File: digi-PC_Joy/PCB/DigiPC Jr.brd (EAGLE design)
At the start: 42.7 x 24.8 mm, 7 parts

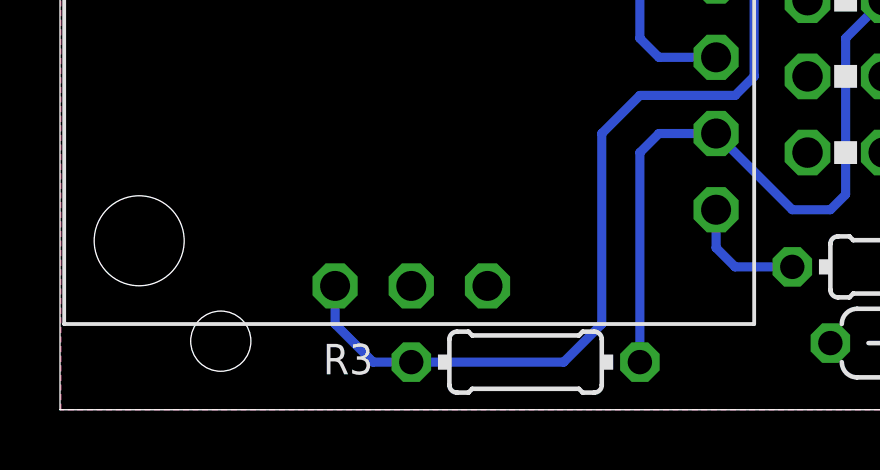
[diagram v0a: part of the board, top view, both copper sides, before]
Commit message: Updadet footprint of digispark board with USB connector
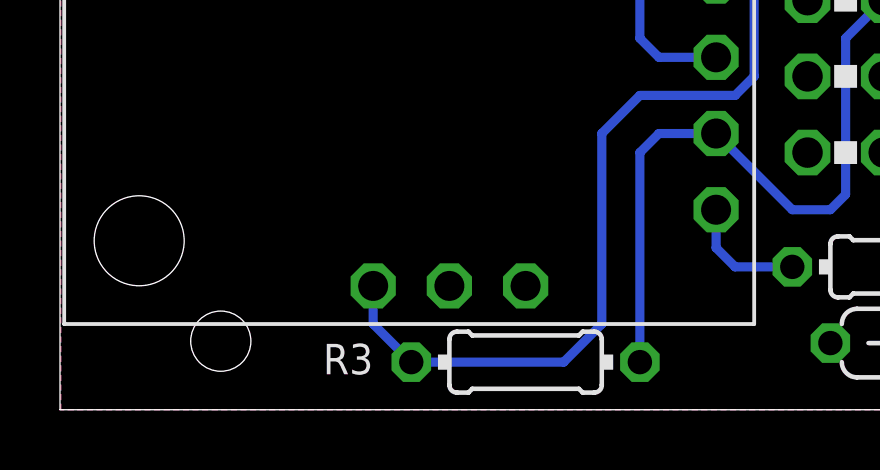
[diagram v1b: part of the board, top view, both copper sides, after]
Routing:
- net VCC: track 29.2 -> 28.0 mm
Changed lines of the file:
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@@
 <contactref element="R3" pad="2"/>
 <contactref element="B1" pad="5V"/>
-<wire x1="16.51" y1="12.065" x2="16.51" y2="10.795" width="0.3048" layer="16"/>
-<wire x1="16.51" y1="10.795" x2="17.78" y2="9.525" width="0.3048" layer="16"/>
-<wire x1="17.78" y1="9.525" x2="19.05" y2="9.525" width="0.3048" layer="16"/>
+<wire x1="17.78" y1="12.065" x2="17.78" y2="10.795" width="0.3048" layer="16"/>
+<wire x1="17.78" y1="10.795" x2="19.05" y2="9.525" width="0.3048" layer="16"/>
 <wire x1="32.258" y1="24.13" x2="30.48" y2="22.352" width="0.3048" layer="16"/>
 <wire x1="30.48" y1="22.352" x2="30.48" y2="19.05" width="0.3048" layer="16"/>

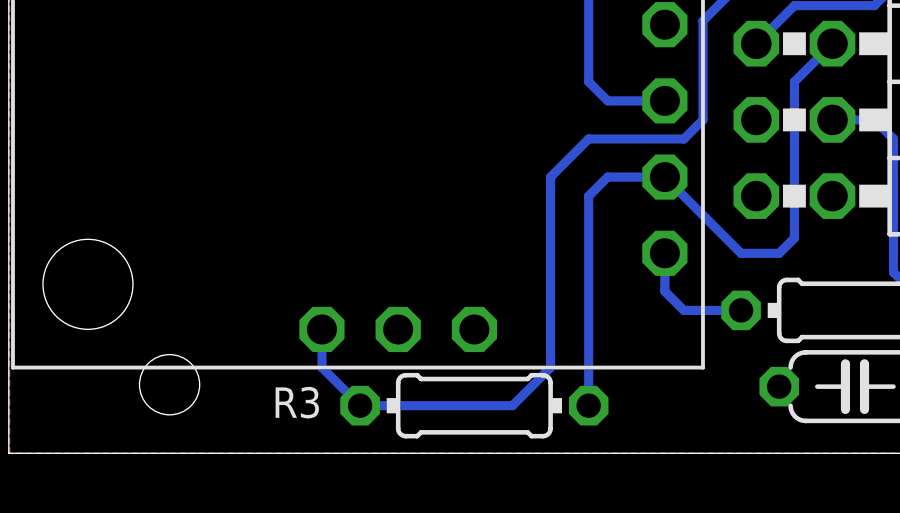
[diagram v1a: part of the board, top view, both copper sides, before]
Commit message: updated digispark footprint
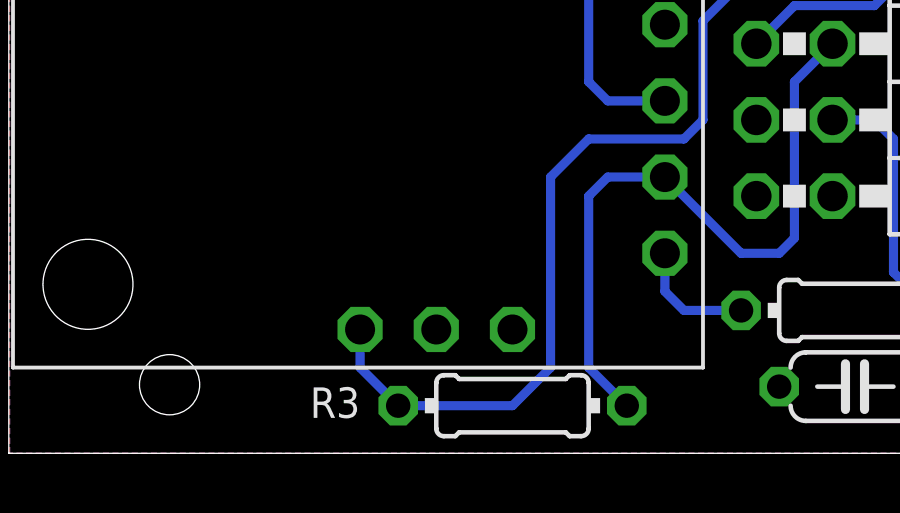
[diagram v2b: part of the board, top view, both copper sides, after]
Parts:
- moved R3 1.27 mm to (24.1, 9.53)
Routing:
- net VCC: track 28.0 -> 26.7 mm
- net S2: track 22.4 -> 22.9 mm
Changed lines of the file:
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@@
 <attribute name="VALUE" x="34.5694" y="27.4574" size="1.016" layer="27" ratio="10"/>
 </element>
-<element name="R3" library="rcl" package="0204/7" value="560" x="22.86" y="9.525" smashed="yes" rot="R180">
-<attribute name="NAME" x="17.78" y="10.1346" size="1.016" layer="25" ratio="10" rot="R180"/>
-<attribute name="VALUE" x="21.8694" y="9.0424" size="1.016" layer="27" ratio="10"/>
+<element name="R3" library="rcl" package="0204/7" value="560" x="24.13" y="9.525" smashed="yes" rot="R180">
+<attribute name="NAME" x="19.05" y="10.1346" size="1.016" layer="25" ratio="10" rot="R180"/>
+<attribute name="VALUE" x="23.1394" y="9.0424" size="1.016" layer="27" ratio="10"/>
 </element>
 <element name="B1" library="Digistump" package="DIGISPARK_SOCKET" value="" x="30.48" y="29.845" smashed="yes" rot="R270">
@@
 <contactref element="R3" pad="2"/>
 <contactref element="B1" pad="5V"/>
-<wire x1="17.78" y1="12.065" x2="17.78" y2="10.795" width="0.3048" layer="16"/>
-<wire x1="17.78" y1="10.795" x2="19.05" y2="9.525" width="0.3048" layer="16"/>
+<wire x1="19.05" y1="12.065" x2="19.05" y2="10.795" width="0.3048" layer="16"/>
+<wire x1="19.05" y1="10.795" x2="20.32" y2="9.525" width="0.3048" layer="16"/>
 <wire x1="32.258" y1="24.13" x2="30.48" y2="22.352" width="0.3048" layer="16"/>
 <wire x1="30.48" y1="22.352" x2="30.48" y2="19.05" width="0.3048" layer="16"/>
@@
 <wire x1="25.4" y1="17.145" x2="25.4" y2="10.795" width="0.3048" layer="16"/>
 <wire x1="25.4" y1="10.795" x2="24.13" y2="9.525" width="0.3048" layer="16"/>
-<wire x1="24.13" y1="9.525" x2="19.05" y2="9.525" width="0.3048" layer="16"/>
+<wire x1="24.13" y1="9.525" x2="20.32" y2="9.525" width="0.3048" layer="16"/>
 </signal>
 <signal name="RY">
@@
 <contactref element="B1" pad="P1"/>
 <wire x1="34.798" y1="21.59" x2="33.528" y2="20.32" width="0.3048" layer="16"/>
-<wire x1="26.67" y1="9.525" x2="26.67" y2="16.51" width="0.3048" layer="16"/>
+<wire x1="27.94" y1="9.525" x2="26.67" y2="10.795" width="0.3048" layer="16"/>
+<wire x1="26.67" y1="10.795" x2="26.67" y2="16.51" width="0.3048" layer="16"/>
 <wire x1="26.67" y1="16.51" x2="27.305" y2="17.145" width="0.3048" layer="16"/>
 <wire x1="27.305" y1="17.145" x2="29.21" y2="17.145" width="0.3048" layer="16"/>
